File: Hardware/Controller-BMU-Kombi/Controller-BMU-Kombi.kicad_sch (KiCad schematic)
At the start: 18 parts, among them J1 Conn_01x05_Socket, J2 Conn_01x05_Socket, J3 Conn_01x05_Socket, J4 Conn_01x05_Socket, J5 Conn_01x05_Socket, J6 Conn_01x05_Socket

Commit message: updated
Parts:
- removed U2: ~, symbol Batteriestecker:Batteriestecker
- added BT2: BK-18650-PC8, BK-18650-PC8:BAT_BK-18650-PC8, symbol BK-18650-PC8:BK-18650-PC8
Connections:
- net CELLS+: now reaches J1.4 (Pin_4), TP1.1
- net CELLS+: now also BT2.1+
- net CELLS-: now reaches J4.5 (Pin_5), TP8.1
- net CELLS-: now also BT2.4-
- new net: BT2.1-, BT2.2+
- new net: BT2.2-, BT2.3+
- new net: BT2.3-, BT2.4+
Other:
- note added: "18650-Li-Ionen-Zellen"

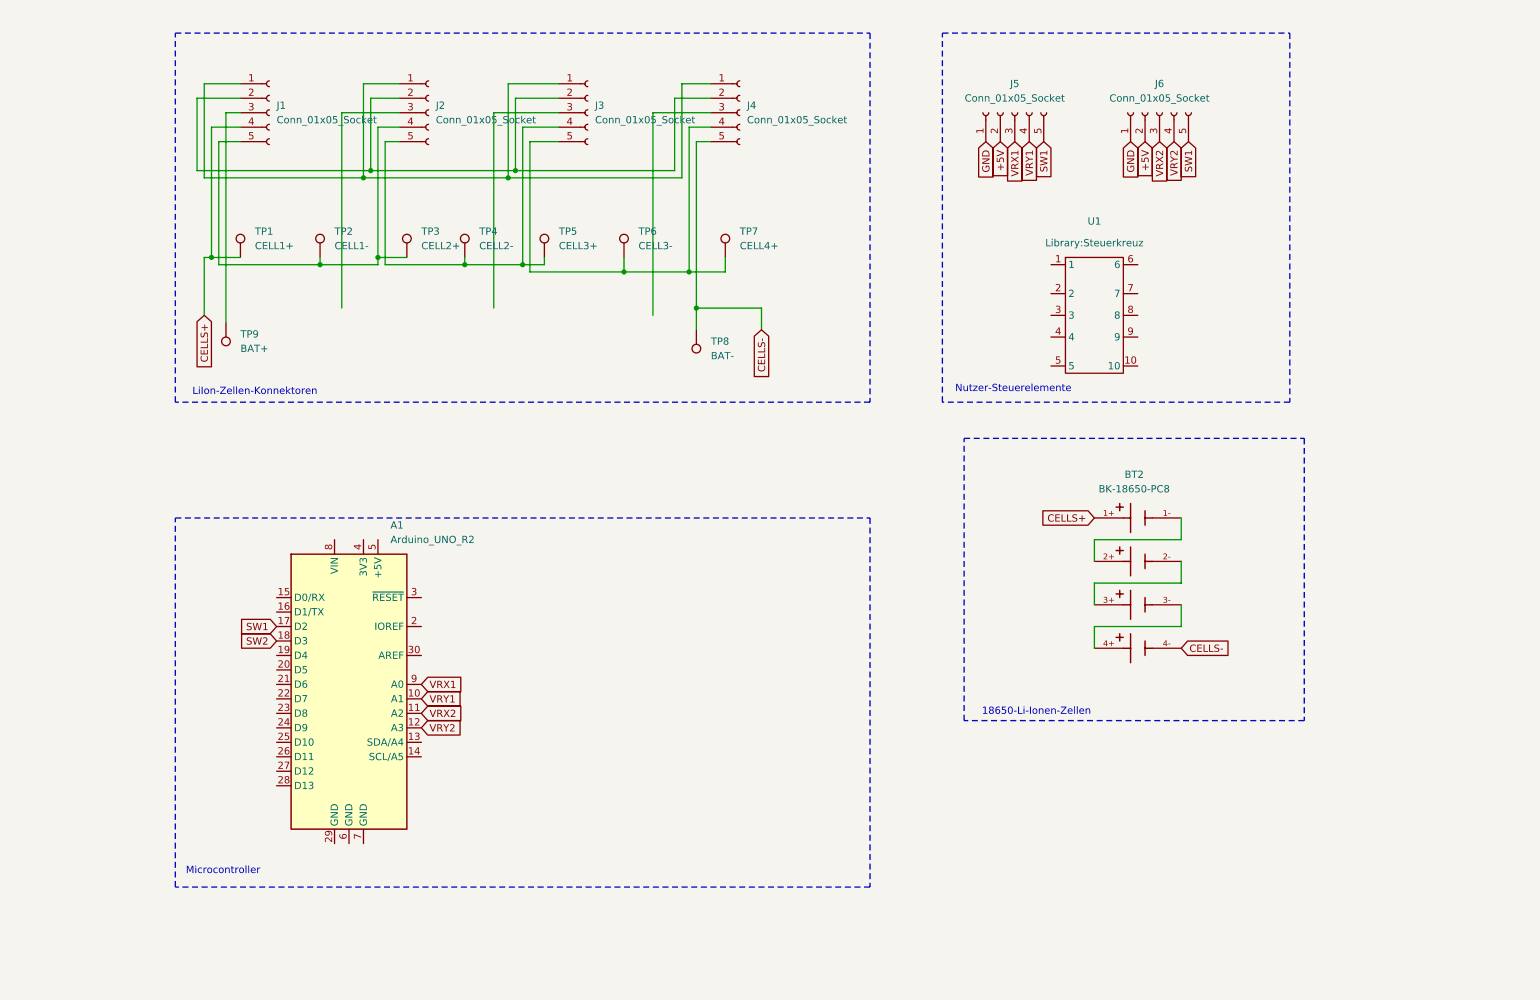
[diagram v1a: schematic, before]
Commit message: added circuitry for user controls
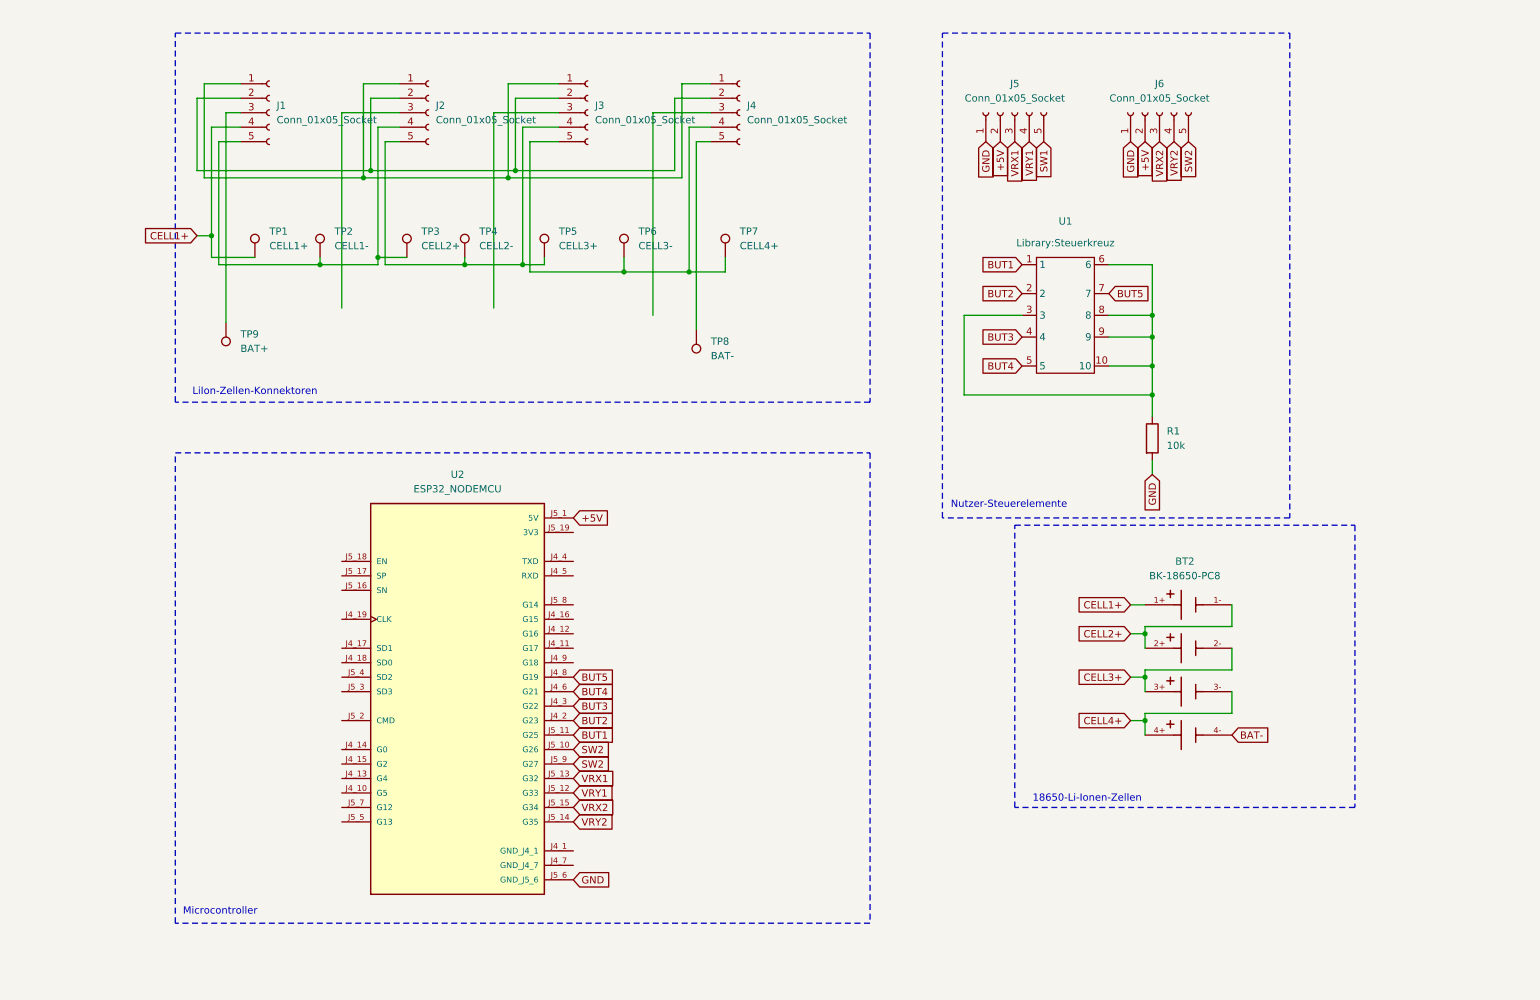
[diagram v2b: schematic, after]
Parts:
- removed A1: Arduino_UNO_R2, Module:Arduino_UNO_R2, symbol MCU_Module:Arduino_UNO_R2
- added R1: 10k, Resistor_SMD:R_1206_3216Metric, symbol Device:R
- added U2: ESP32_NODEMCU, ESP32_NODEMCU:MODULE_ESP32_NODEMCU, symbol ESP32_NODEMCU:ESP32_NODEMCU
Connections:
- net +5V: now also U2.J5_1 (5V)
- net GND: now also R1.2, U2.J5_6 (GND_J5_6)
- net SW1: no longer J6.5 (Pin_5)
- net SW2: now also J6.5 (Pin_5), U2.J5_10 (G26), U2.J5_9 (G27)
- net VRX1: now also U2.J5_13 (G32)
- net VRX2: now also U2.J5_15 (G34)
- net VRY1: now also U2.J5_12 (G33)
- net VRY2: now also U2.J5_14 (G35)
- net CELL2+: now reaches BT2.1-, BT2.2+
- net CELL3+: now reaches BT2.2-, BT2.3+
- net CELL4+: now reaches BT2.3-, BT2.4+
- net BUT1: now reaches U1.1
- net BUT1: now also U2.J5_11 (G25)
- net at U1.10: now also U1.3, U1.6, U1.8, U1.9, R1.1
- net BUT2: now reaches U1.2
- net BUT2: now also U2.J4_2 (G23)
- net BUT3: now reaches U1.4
- net BUT3: now also U2.J4_3 (G22)
- net BUT4: now reaches U1.5
- net BUT4: now also U2.J4_6 (G21)
- net BUT5: now reaches U1.7
- net BUT5: now also U2.J4_8 (G19)
- net CELLS+ renamed CELL1+
- net CELLS-: no longer names the net of J4.5 (Pin_5), TP8.1
- net CELLS-: no longer BT2.4-
- new net BAT-: BT2.4-
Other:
- moved on the sheet: BT2, TP1, U1

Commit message: synchronizing
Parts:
- removed TP1: CELL1+, Connector_Pin:Pin_D1.0mm_L10.0mm, symbol Connector:TestPoint
- removed TP2: CELL1-, Connector_Pin:Pin_D1.0mm_L10.0mm, symbol Connector:TestPoint
- removed TP3: CELL2+, Connector_Pin:Pin_D1.0mm_L10.0mm, symbol Connector:TestPoint
- removed TP4: CELL2-, Connector_Pin:Pin_D1.0mm_L10.0mm, symbol Connector:TestPoint
- removed TP5: CELL3+, Connector_Pin:Pin_D1.0mm_L10.0mm, symbol Connector:TestPoint
- removed TP6: CELL3-, Connector_Pin:Pin_D1.0mm_L10.0mm, symbol Connector:TestPoint
- removed TP7: CELL4+, Connector_Pin:Pin_D1.0mm_L10.0mm, symbol Connector:TestPoint

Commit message: updates
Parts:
- removed BT2: BK-18650-PC8, BK-18650-PC8:BAT_BK-18650-PC8, symbol BK-18650-PC8:BK-18650-PC8
- removed TP8: BAT-, Connector_Pin:Pin_D1.0mm_L10.0mm, symbol Connector:TestPoint
- removed TP9: BAT+, Connector_Pin:Pin_D1.0mm_L10.0mm, symbol Connector:TestPoint
- added U3, U4, U5, U6, U7, U8: ~, Batteriestecker:Batteriestecker, symbol Batteriestecker:Batteriestecker
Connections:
- net +5V: now also U8.1 (BAT+)
- net CELL1+: now also U4.1 (BAT+)
- net CELL2+: now also J1.5 (Pin_5), J2.4 (Pin_4), U4.2 (BAT-), U5.1 (BAT+)
- net CELL3+: now also J2.5 (Pin_5), J3.4 (Pin_4), U5.2 (BAT-), U6.1 (BAT+)
- net CELL4+: now also J3.5 (Pin_5), J4.4 (Pin_4), U6.2 (BAT-), U7.1 (BAT+)
- net GND: now also U8.2 (BAT-)
- net at J1.3 (Pin_3): now also U3.1 (BAT+)
- net CELL4-: now reaches J4.5 (Pin_5)
- net CELL4-: now also U3.2 (BAT-), U7.2 (BAT-)
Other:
- note added: "BMU-Konnektoren"
- note removed: "LiIon-Zellen-Konnektoren"

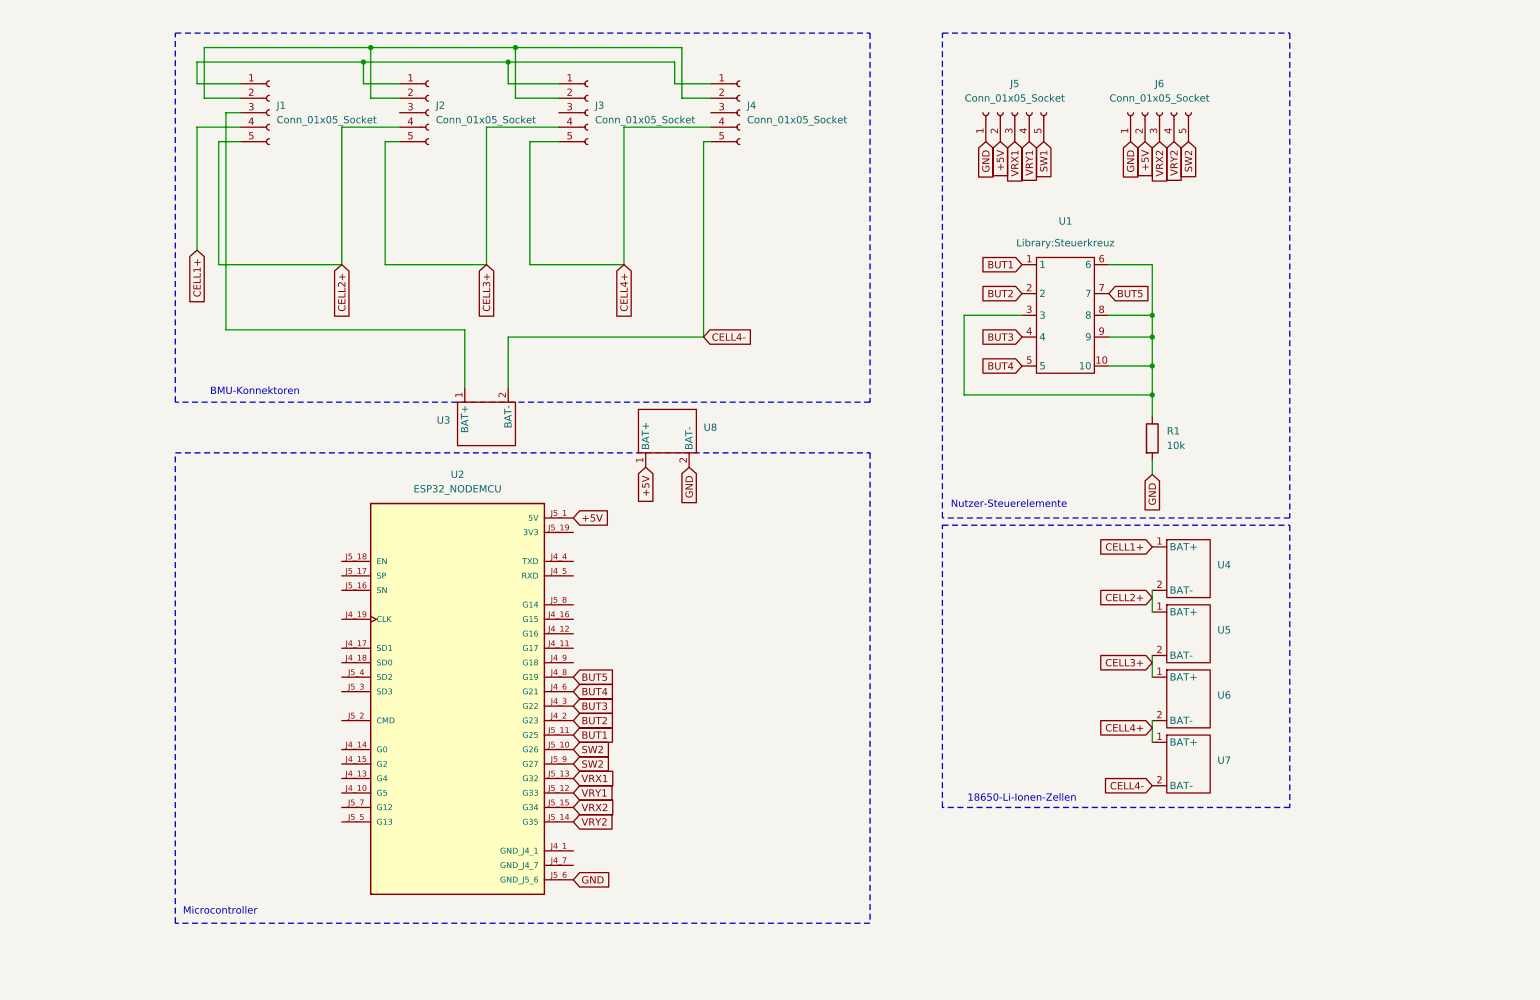
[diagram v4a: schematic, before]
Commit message: added servo connectors
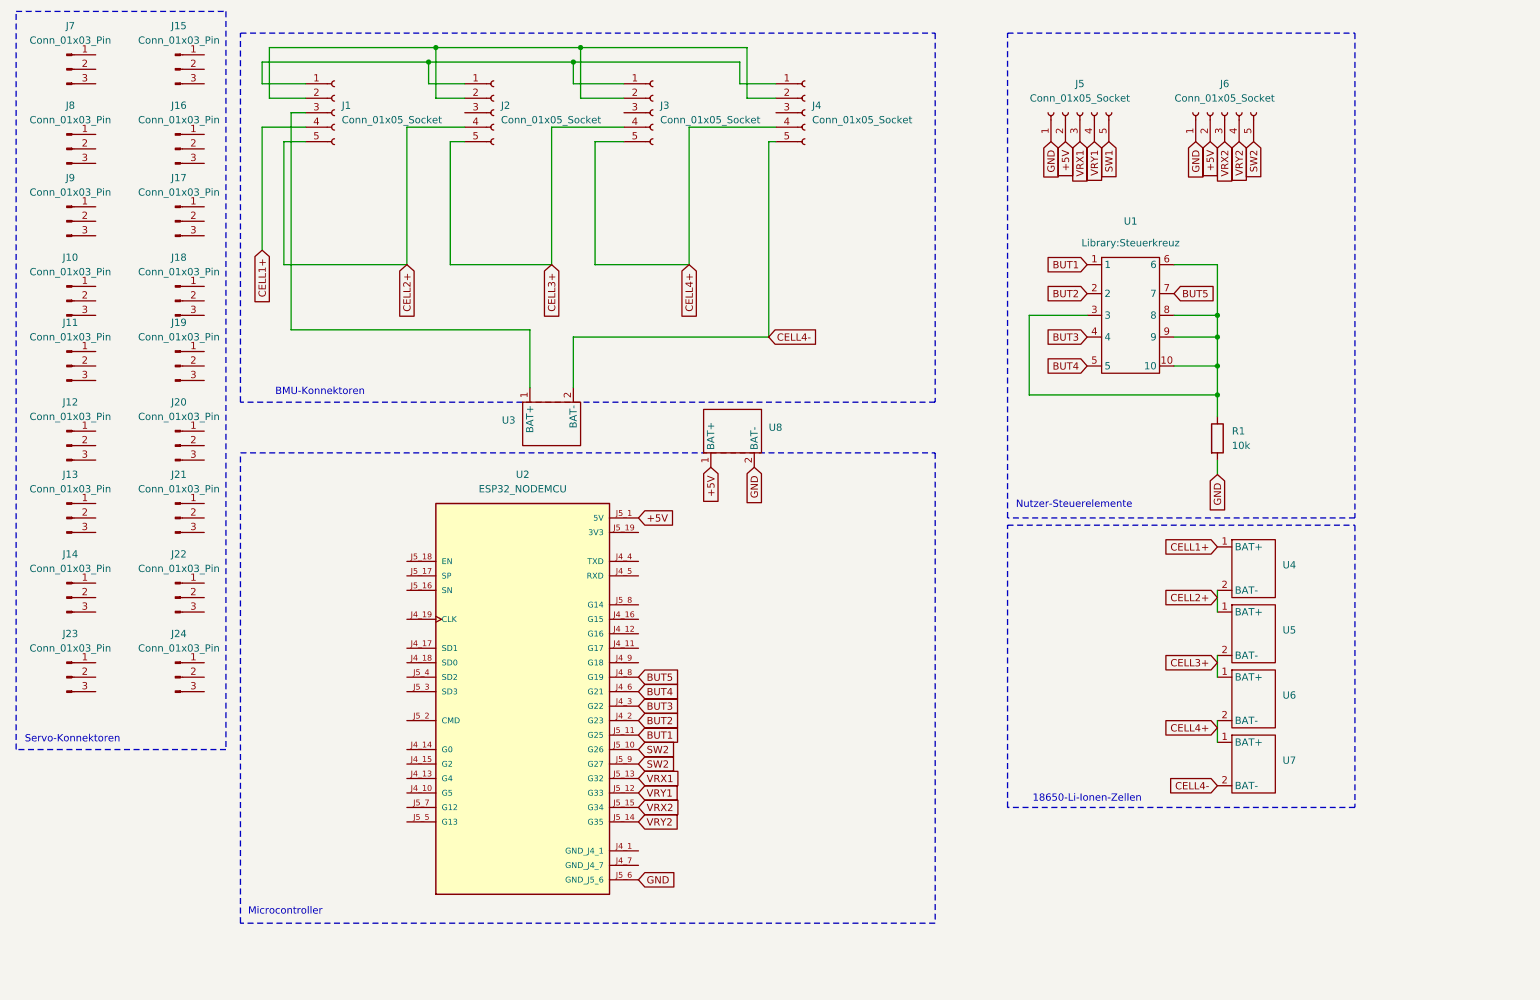
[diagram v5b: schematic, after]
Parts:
- added J10, J11, J12, J13, J14, J15, J16, J17, J18, J19, J20, J21, J22, J23, J24, J7, J8, J9: Conn_01x03_Pin, Connector_PinHeader_2.54mm:PinHeader_1x03_P2.54mm_Vertical, symbol Connector:Conn_01x03_Pin
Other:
- note added: "Servo-Konnektoren"
- moved on the sheet: J1, J2, J3, J4, J5, J6, R1, U1, U2, U3, U4, U5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

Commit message: added rf connectors, changed a few net labels
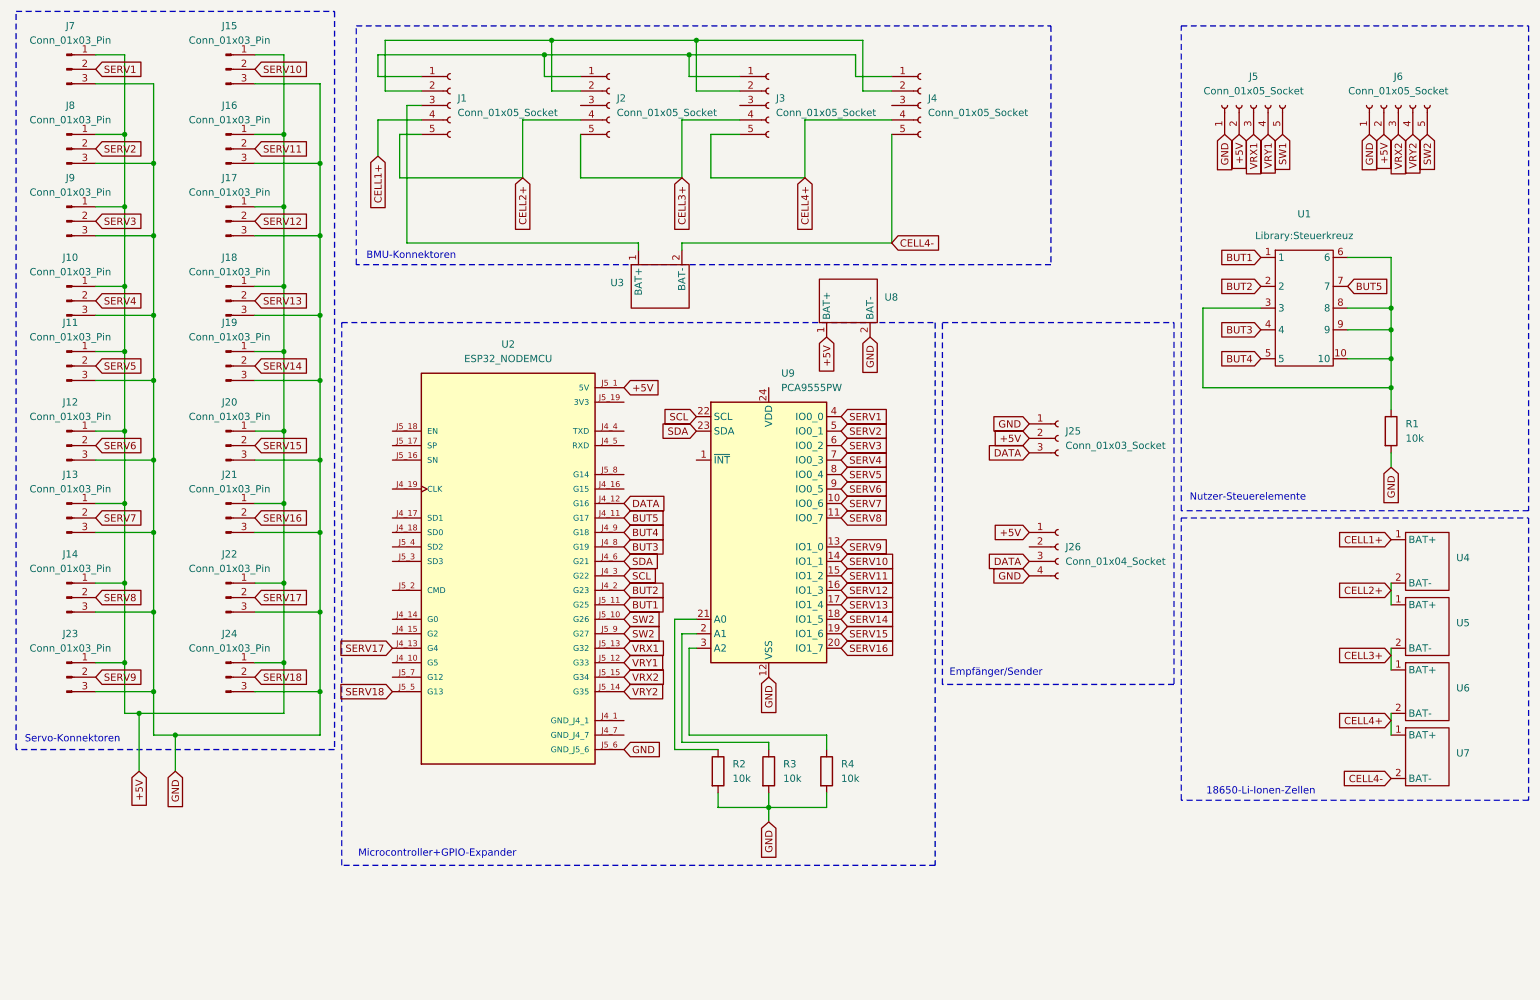
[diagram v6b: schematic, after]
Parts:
- added J25: Conn_01x03_Socket, Connector_PinSocket_2.54mm:PinSocket_1x03_P2.54mm_Horizontal, symbol Connector:Conn_01x03_Socket
- added J26: Conn_01x04_Socket, Connector_PinSocket_2.54mm:PinSocket_1x04_P2.54mm_Horizontal, symbol Connector:Conn_01x04_Socket
- added R2, R3, R4: 10k, Resistor_SMD:R_1206_3216Metric, symbol Device:R
- added U9: PCA9555PW, Package_SO:TSSOP-24_4.4x7.8mm_P0.65mm, symbol Interface_Expansion:PCA9555PW
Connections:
- net +5V: now also J10.1 (Pin_1), J11.1 (Pin_1), J12.1 (Pin_1), J13.1 (Pin_1), J14.1 (Pin_1), J15.1 (Pin_1), J16.1 (Pin_1), J17.1 (Pin_1), J18.1 (Pin_1), J19.1 (Pin_1), J20.1 (Pin_1), J21.1 (Pin_1), J22.1 (Pin_1), J23.1 (Pin_1), J24.1 (Pin_1), J7.1 (Pin_1), J8.1 (Pin_1), J9.1 (Pin_1), J25.2 (Pin_2), J26.1 (Pin_1)
- net BUT3: now also U2.J4_8 (G19); no longer U2.J4_3 (G22)
- net BUT4: now also U2.J4_9 (G18); no longer U2.J4_6 (G21)
- net BUT5: now also U2.J4_11 (G17); no longer U2.J4_8 (G19)
- net GND: now also J10.3 (Pin_3), J11.3 (Pin_3), J12.3 (Pin_3), J13.3 (Pin_3), J14.3 (Pin_3), J15.3 (Pin_3), J16.3 (Pin_3), J17.3 (Pin_3), J18.3 (Pin_3), J19.3 (Pin_3), J20.3 (Pin_3), J21.3 (Pin_3), J22.3 (Pin_3), J23.3 (Pin_3), J24.3 (Pin_3), J7.3 (Pin_3), J8.3 (Pin_3), J9.3 (Pin_3), J25.1 (Pin_1), J26.4 (Pin_4), R2.2, R3.2, R4.2, U9.12 (VSS)
- net SERV1: now reaches J7.2 (Pin_2)
- net SERV1: now also U9.4 (IO0_0)
- net SERV8: now reaches J14.2 (Pin_2)
- net SERV8: now also U9.11 (IO0_7)
- net SERV3: now reaches J9.2 (Pin_2)
- net SERV3: now also U9.6 (IO0_2)
- net SERV11: now reaches J16.2 (Pin_2)
- net SERV11: now also U9.15 (IO1_2)
- net SERV9: now reaches J23.2 (Pin_2)
- net SERV9: now also U9.13 (IO1_0)
- net SERV15: now reaches J20.2 (Pin_2)
- net SERV15: now also U9.19 (IO1_6)
- net SERV18: now reaches J24.2 (Pin_2)
- net SERV18: now also U2.J5_5 (G13)
- net SERV13: now reaches J18.2 (Pin_2)
- net SERV13: now also U9.17 (IO1_4)
- net SERV10: now reaches J15.2 (Pin_2)
- net SERV10: now also U9.14 (IO1_1)
- net SERV2: now reaches J8.2 (Pin_2)
- net SERV2: now also U9.5 (IO0_1)
- net SERV7: now reaches J13.2 (Pin_2)
- net SERV7: now also U9.10 (IO0_6)
- net DATA: now reaches U2.J4_12 (G16)
- net DATA: now also J25.3 (Pin_3), J26.3 (Pin_3)
- net SERV17: now reaches U2.J4_13 (G4)
- net SERV17: now also J22.2 (Pin_2)
- net SERV4: now reaches J10.2 (Pin_2)
- net SERV4: now also U9.7 (IO0_3)
- net SERV16: now reaches J21.2 (Pin_2)
- net SERV16: now also U9.20 (IO1_7)
- net SERV14: now reaches J19.2 (Pin_2)
- net SERV14: now also U9.18 (IO1_5)
- net SERV6: now reaches J12.2 (Pin_2)
- net SERV6: now also U9.9 (IO0_5)
- net SERV5: now reaches J11.2 (Pin_2)
- net SERV5: now also U9.8 (IO0_4)
- net SERV12: now reaches J17.2 (Pin_2)
- net SERV12: now also U9.16 (IO1_3)
- new net: R4.1, U9.3 (A2)
- new net: R3.1, U9.2 (A1)
- new net: R2.1, U9.21 (A0)
- new net SCL: U2.J4_3 (G22), U9.22 (SCL)
- new net SDA: U2.J4_6 (G21), U9.23 (SDA)
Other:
- note added: "Empfänger/Sender"
- note added: "Microcontroller+GPIO-Expander"
- note removed: "Microcontroller"
- moved on the sheet: J1, J15, J16, J17, J18, J19, J2, J20, J21, J22, J24, J3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

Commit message: general pcb layout
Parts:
- added U10, U11, U12, U13: ~, BMU:BMU, symbol BMU:BMU
- added U14: ~, Lokale Bibliothek:Empfänger, symbol Lokale Bibliothek:Empfänger
- added U15: ~, Lokale Bibliothek:Sender, symbol Lokale Bibliothek:Sender
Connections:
- net +5V: now also J26.4 (Pin_4); no longer J26.1 (Pin_1)
- net DATA: now also J26.2 (Pin_2)
- net GND: now also J26.1 (Pin_1); no longer J26.4 (Pin_4)
